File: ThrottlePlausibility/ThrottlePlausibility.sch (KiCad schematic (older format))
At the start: 18 parts, among them U1 MCP6004, U2 LM339, U3 74LS08, U4 74LS08, U5 LM339, U6 TLP222A

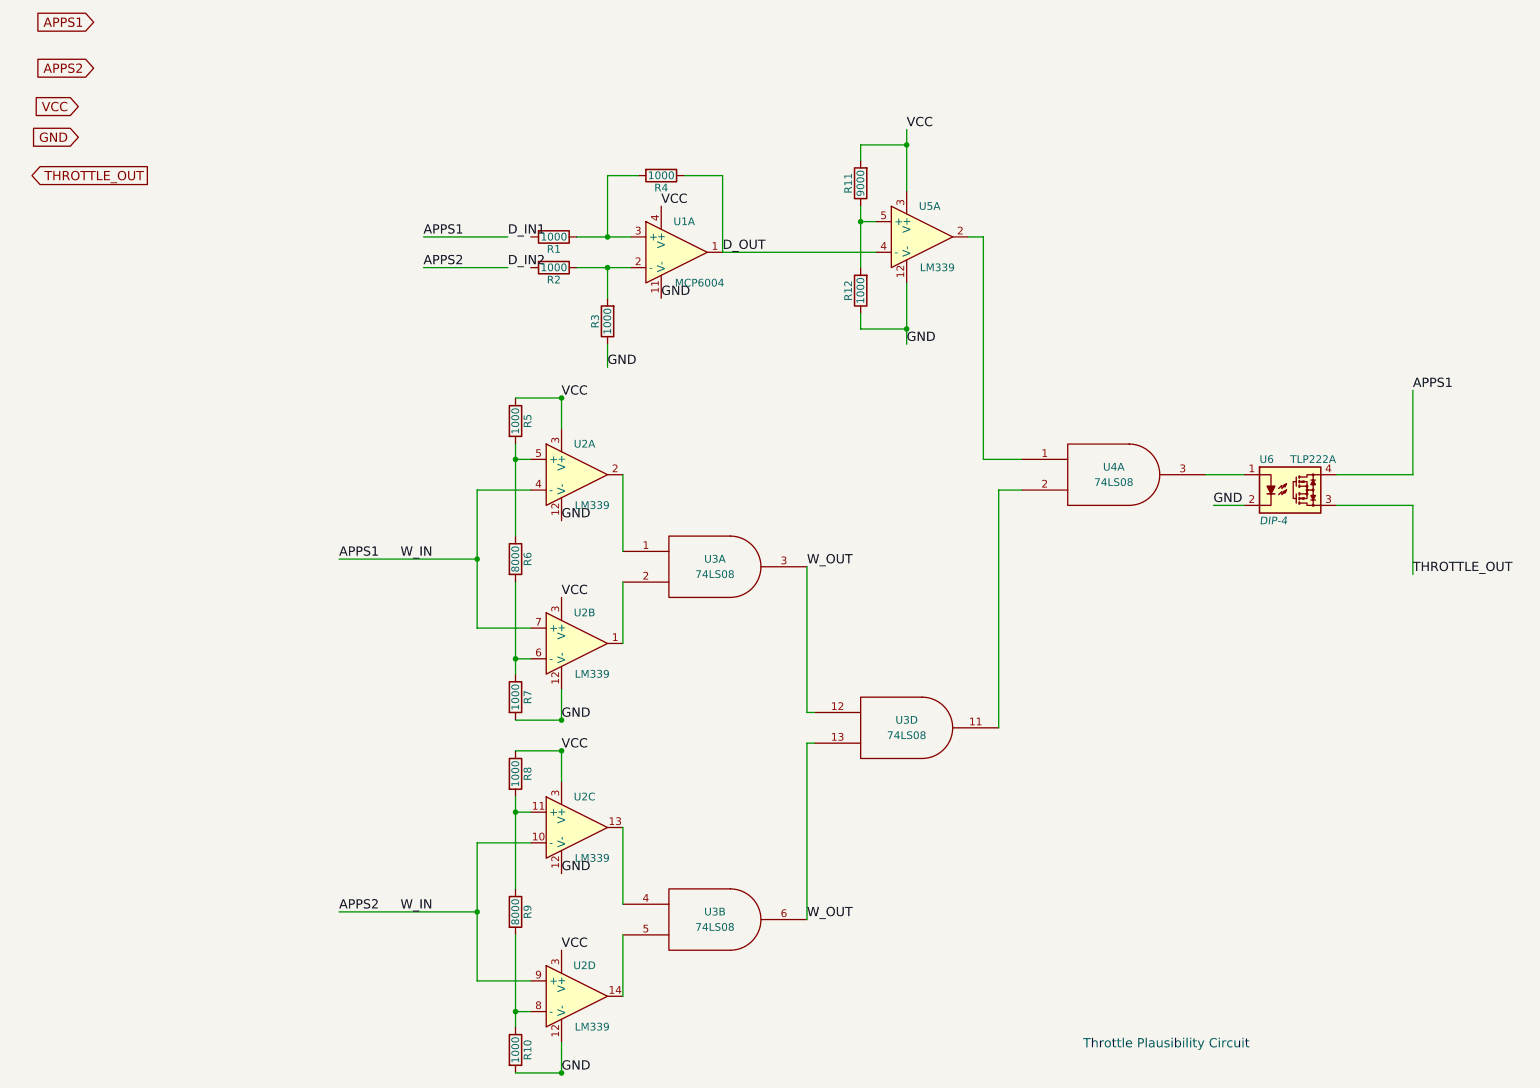
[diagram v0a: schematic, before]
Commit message: added SPICE model
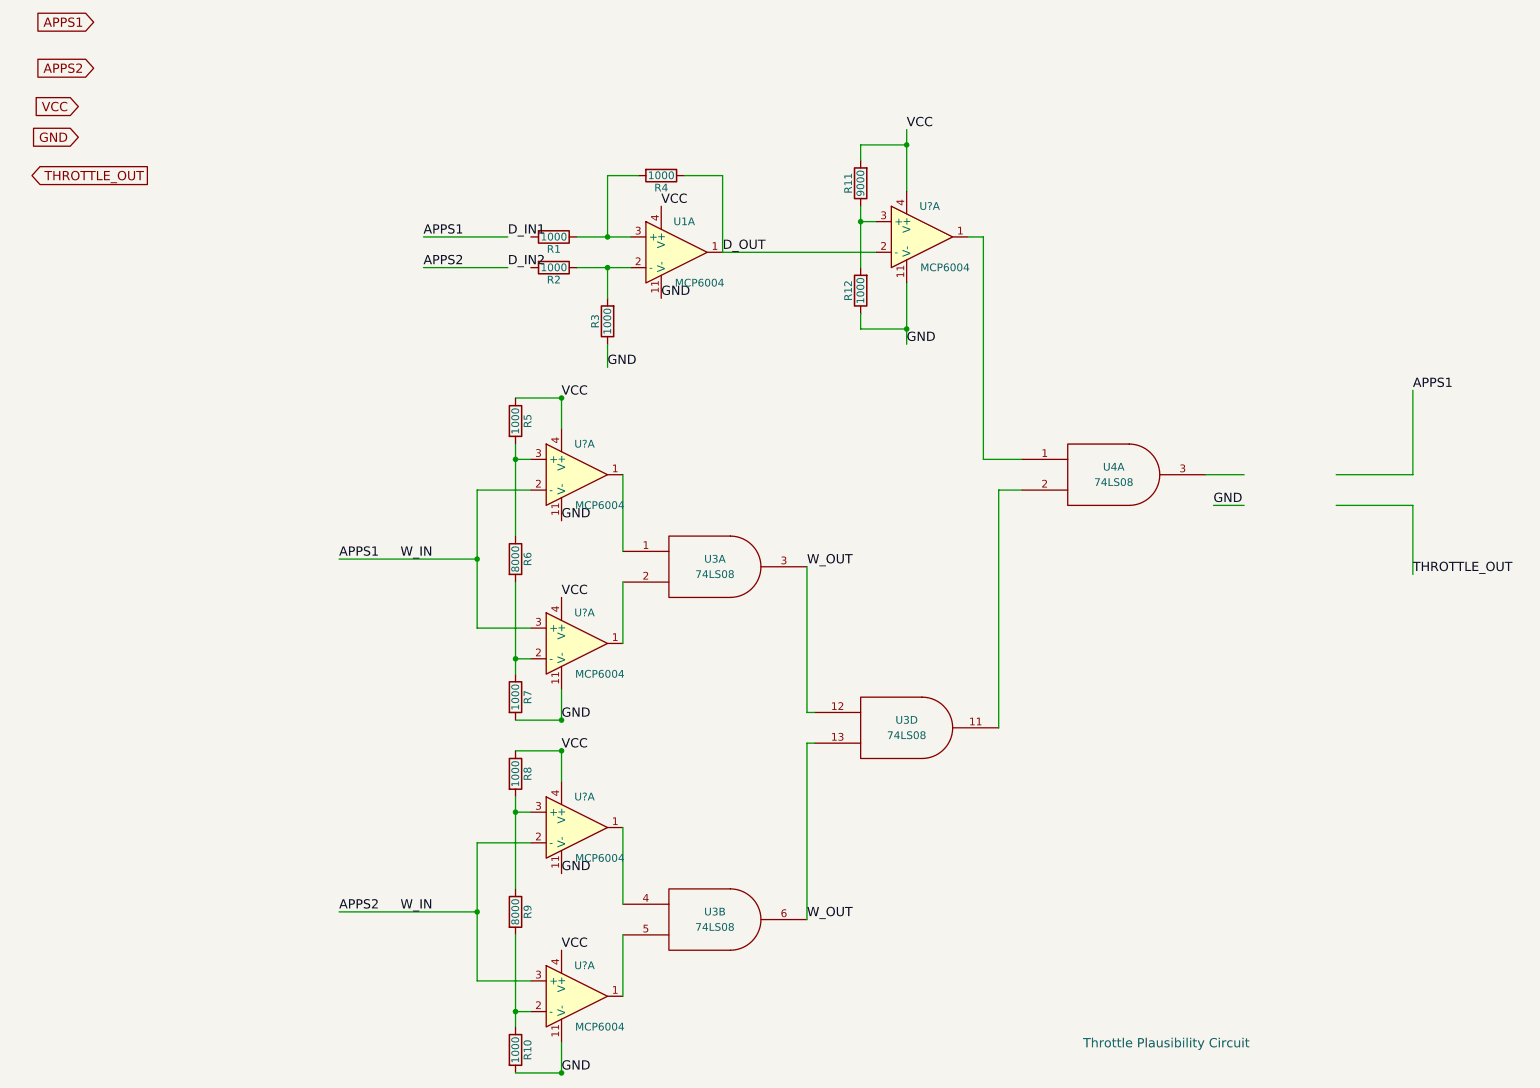
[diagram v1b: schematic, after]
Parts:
- removed U2, U5: LM339, symbol LM339
- removed U6: TLP222A, DIP-4, symbol TLP222A
- added U? (x5): MCP6004, symbol MCP6004
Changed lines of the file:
@@
 Text Label 3100 2400 0    60   ~ 0
 APPS2
-$Comp
-L LM339 U5
-U 1 1 589C6EA7
-P 6350 2200
-F 0 "U5" H 6400 2400 50  0000 C CNN
-F 1 "LM339" H 6450 2000 50  0000 C CNN
-F 2 "" H 6300 2300 50  0000 C CNN
-F 3 "" H 6400 2400 50  0000 C CNN
-	1    6350 2200
-	1    0    0    -1
-$EndComp
-$Comp
-L LM339 U2
-U 2 1 589C9450
-P 4100 4850
-F 0 "U2" H 4150 5050 50  0000 C CNN
-F 1 "LM339" H 4200 4650 50  0000 C CNN
-F 2 "" H 4050 4950 50  0000 C CNN
-F 3 "" H 4150 5050 50  0000 C CNN
-	2    4100 4850
-	1    0    0    -1
-$EndComp
-$Comp
-L LM339 U2
-U 1 1 589C95FE
-P 4100 3750
-F 0 "U2" H 4150 3950 50  0000 C CNN
-F 1 "LM339" H 4200 3550 50  0000 C CNN
-F 2 "" H 4050 3850 50  0000 C CNN
-F 3 "" H 4150 3950 50  0000 C CNN
-	1    4100 3750
-	1    0    0    -1
-$EndComp
-$Comp
-L LM339 U2
-U 3 1 589C96D1
-P 4100 6050
-F 0 "U2" H 4150 6250 50  0000 C CNN
-F 1 "LM339" H 4200 5850 50  0000 C CNN
-F 2 "" H 4050 6150 50  0000 C CNN
-F 3 "" H 4150 6250 50  0000 C CNN
-	3    4100 6050
-	1    0    0    -1
-$EndComp
-$Comp
-L LM339 U2
-U 4 1 589C974C
-P 4100 7150
-F 0 "U2" H 4150 7350 50  0000 C CNN
-F 1 "LM339" H 4200 6950 50  0000 C CNN
-F 2 "" H 4050 7250 50  0000 C CNN
-F 3 "" H 4150 7350 50  0000 C CNN
-	4    4100 7150
-	1    0    0    -1
-$EndComp
-$Comp
-L TLP222A U6
-U 1 1 589CAD48
-P 8750 3850
-F 0 "U6" H 8550 4050 50  0000 L CNN
-F 1 "TLP222A" H 8750 4050 50  0000 L CNN
-F 2 "DIP-4" H 8550 3650 50  0000 L CIN
-F 3 "" H 8700 3850 50  0000 L CNN
-	1    8750 3850
-	1    0    0    -1
-$EndComp
 Wire Wire Line
 	6750 2200 6750 3650
@@
 Text GLabel 1300 1800 0    60   Output ~ 0
 THROTTLE_OUT
+$Comp
+L MCP6004 U?
+U 1 1 58A1CB70
+P 4100 3750
+F 0 "U?" H 4150 3950 50  0000 C CNN
+F 1 "MCP6004" H 4250 3550 50  0000 C CNN
+F 2 "" H 4050 3850 50  0000 C CNN
+F 3 "" H 4150 3950 50  0000 C CNN
+	1    4100 3750
+	1    0    0    -1
+$EndComp
+$Comp
+L MCP6004 U?
+U 1 1 58A1CCBC
+P 4100 4850
+F 0 "U?" H 4150 5050 50  0000 C CNN
+F 1 "MCP6004" H 4250 4650 50  0000 C CNN
+F 2 "" H 4050 4950 50  0000 C CNN
+F 3 "" H 4150 5050 50  0000 C CNN
+	1    4100 4850
+	1    0    0    -1
+$EndComp
+$Comp
+L MCP6004 U?
+U 1 1 58A1D021
+P 4100 6050
+F 0 "U?" H 4150 6250 50  0000 C CNN
+F 1 "MCP6004" H 4250 5850 50  0000 C CNN
+F 2 "" H 4050 6150 50  0000 C CNN
+F 3 "" H 4150 6250 50  0000 C CNN
+	1    4100 6050
+	1    0    0    -1
+$EndComp
+$Comp
+L MCP6004 U?
+U 1 1 58A1D0D5
+P 4100 7150
+F 0 "U?" H 4150 7350 50  0000 C CNN
+F 1 "MCP6004" H 4250 6950 50  0000 C CNN
+F 2 "" H 4050 7250 50  0000 C CNN
+F 3 "" H 4150 7350 50  0000 C CNN
+	1    4100 7150
+	1    0    0    -1
+$EndComp
+$Comp
+L MCP6004 U?
+U 1 1 58A1D98F
+P 6350 2200
+F 0 "U?" H 6400 2400 50  0000 C CNN
+F 1 "MCP6004" H 6500 2000 50  0000 C CNN
+F 2 "" H 6300 2300 50  0000 C CNN
+F 3 "" H 6400 2400 50  0000 C CNN
+	1    6350 2200
+	1    0    0    -1
+$EndComp
 $EndSCHEMATC

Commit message: started datasheet text file, altered throttle sch
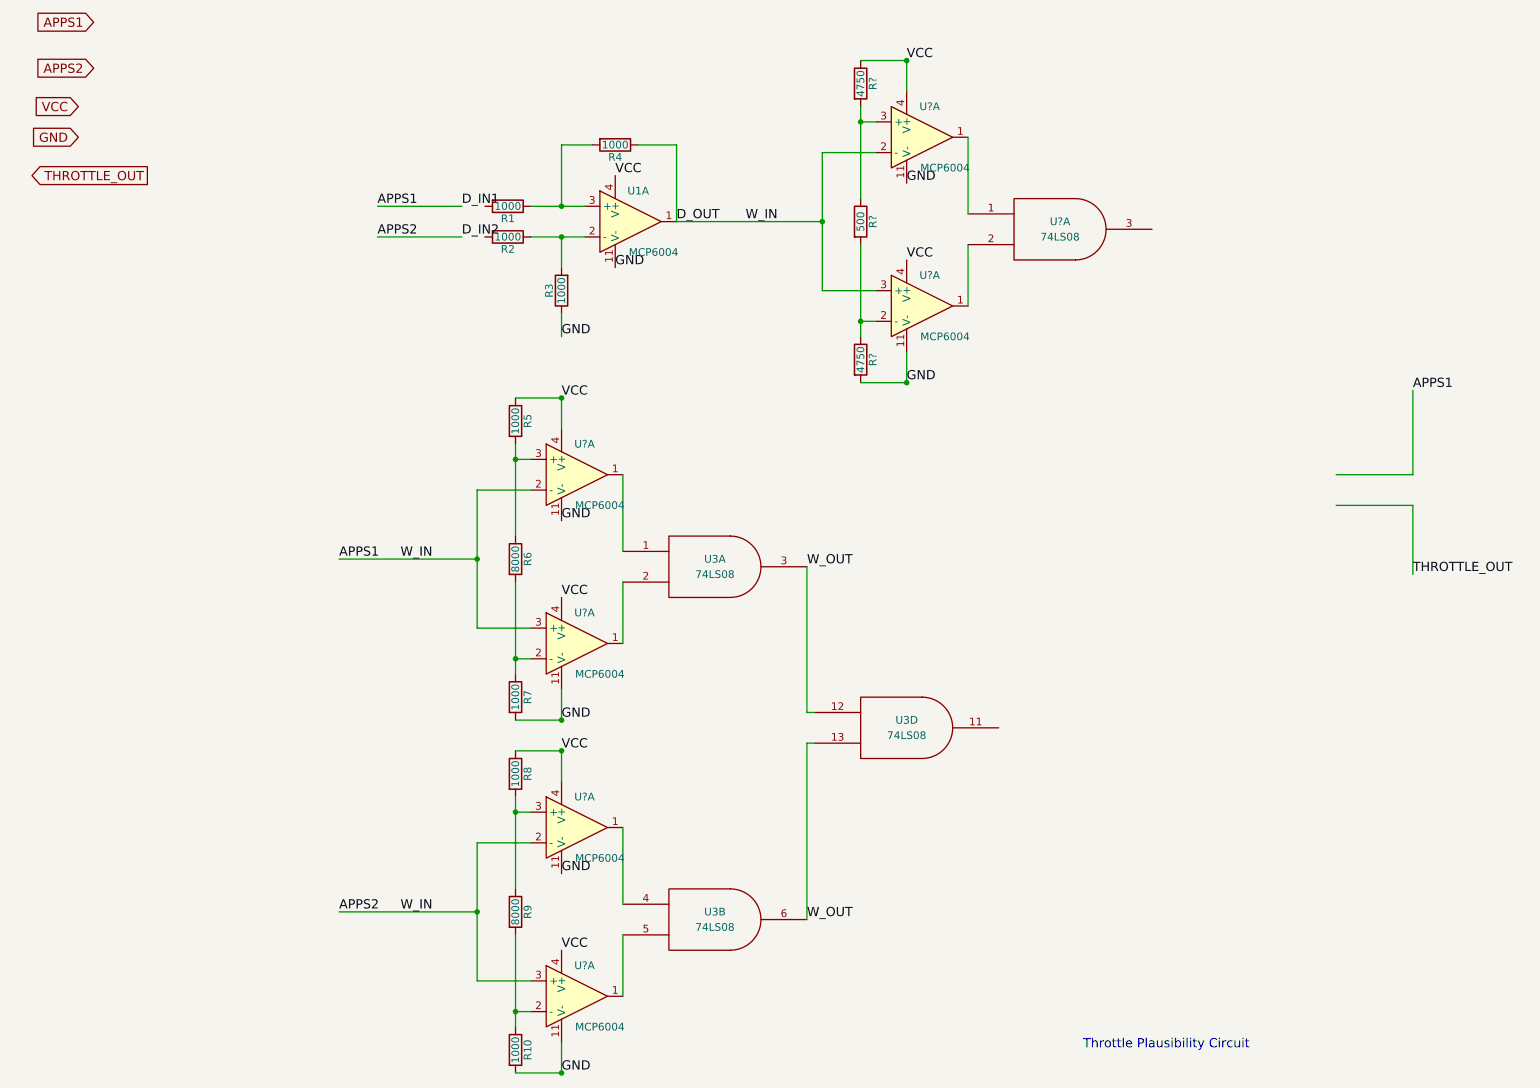
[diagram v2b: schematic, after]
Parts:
- removed R11: 9000, symbol R
- removed R12: 1000, symbol R
- removed U4: 74LS08, symbol 74LS08
- removed U?: MCP6004, symbol MCP6004
- added R? (x2): 4750, symbol R
- added R?: 500, symbol R
- added U?: 74LS08, symbol 74LS08
- added U? (x2): MCP6004, symbol MCP6004
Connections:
- wire segments 62 -> 60
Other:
- moved on the sheet: R1, R2, R3, R4, U1A
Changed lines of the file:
@@
 EESchema Schematic File Version 2
+LIBS:TSI_KiCad_Lib
 LIBS:power
 LIBS:device
@@
 L MCP6004 U1
 U 1 1 5897A753
-P 4750 2300
-F 0 "U1" H 4800 2500 50  0000 C CNN
-F 1 "MCP6004" H 4900 2100 50  0000 C CNN
-F 2 "" H 4700 2400 50  0000 C CNN
-F 3 "" H 4800 2500 50  0000 C CNN
-	1    4750 2300
+P 4450 2100
+F 0 "U1" H 4500 2300 50  0000 C CNN
+F 1 "MCP6004" H 4600 1900 50  0000 C CNN
+F 2 "" H 4400 2200 50  0000 C CNN
+F 3 "" H 4500 2300 50  0000 C CNN
+	1    4450 2100
 	1    0    0    -1
 $EndComp
@@
 L R R1
 U 1 1 5897ADAF
-P 3950 2200
-F 0 "R1" V 4030 2200 50  0000 C CNN
-F 1 "1000" V 3950 2200 50  0000 C CNN
-F 2 "" V 3880 2200 50  0000 C CNN
-F 3 "" H 3950 2200 50  0000 C CNN
-	1    3950 2200
+P 3650 2000
+F 0 "R1" V 3730 2000 50  0000 C CNN
+F 1 "1000" V 3650 2000 50  0000 C CNN
+F 2 "" V 3580 2000 50  0000 C CNN
+F 3 "" H 3650 2000 50  0000 C CNN
+	1    3650 2000
 	0    1    1    0
 $EndComp
@@
 L R R2
 U 1 1 5897AE5B
-P 3950 2400
-F 0 "R2" V 4030 2400 50  0000 C CNN
-F 1 "1000" V 3950 2400 50  0000 C CNN
-F 2 "" V 3880 2400 50  0000 C CNN
-F 3 "" H 3950 2400 50  0000 C CNN
-	1    3950 2400
+P 3650 2200
+F 0 "R2" V 3730 2200 50  0000 C CNN
+F 1 "1000" V 3650 2200 50  0000 C CNN
+F 2 "" V 3580 2200 50  0000 C CNN
+F 3 "" H 3650 2200 50  0000 C CNN
+	1    3650 2200
 	0    1    1    0
 $EndComp
@@
 L R R4
 U 1 1 5897AEA9
-P 4650 1800
-F 0 "R4" V 4730 1800 50  0000 C CNN
-F 1 "1000" V 4650 1800 50  0000 C CNN
-F 2 "" V 4580 1800 50  0000 C CNN
-F 3 "" H 4650 1800 50  0000 C CNN
-	1    4650 1800
+P 4350 1600
+F 0 "R4" V 4430 1600 50  0000 C CNN
+F 1 "1000" V 4350 1600 50  0000 C CNN
+F 2 "" V 4280 1600 50  0000 C CNN
+F 3 "" H 4350 1600 50  0000 C CNN
+	1    4350 1600
 	0    1    1    0
 $EndComp
@@
 L R R3
 U 1 1 5897AF3A
-P 4300 2750
-F 0 "R3" V 4380 2750 50  0000 C CNN
-F 1 "1000" V 4300 2750 50  0000 C CNN
-F 2 "" V 4230 2750 50  0000 C CNN
-F 3 "" H 4300 2750 50  0000 C CNN
-	1    4300 2750
+P 4000 2550
+F 0 "R3" V 4080 2550 50  0000 C CNN
+F 1 "1000" V 4000 2550 50  0000 C CNN
+F 2 "" V 3930 2550 50  0000 C CNN
+F 3 "" H 4000 2550 50  0000 C CNN
+	1    4000 2550
 	-1   0    0    1
 $EndComp
-Text Label 4650 2000 0    60   ~ 0
-VCC
-Text Label 4650 2600 0    60   ~ 0
-GND
-Text Label 5050 2300 0    60   ~ 0
+Text Label 4350 1800 0    60   ~ 0
+VCC
+Text Label 4350 2400 0    60   ~ 0
+GND
+Text Label 4750 2100 0    60   ~ 0
 D_OUT
-Text Label 3650 2200 0    60   ~ 0
+Text Label 3350 2000 0    60   ~ 0
 D_IN1
-Text Label 3650 2400 0    60   ~ 0
+Text Label 3350 2200 0    60   ~ 0
 D_IN2
-Text Label 4300 3050 0    60   ~ 0
-GND
-$Comp
-L 74LS08 U4
-U 1 1 589811F3
-P 7600 3750
-F 0 "U4" H 7600 3800 50  0000 C CNN
-F 1 "74LS08" H 7600 3700 50  0000 C CNN
-F 2 "" H 7600 3750 50  0000 C CNN
-F 3 "" H 7600 3750 50  0000 C CNN
-	1    7600 3750
-	1    0    0    -1
-$EndComp
+Text Label 4000 2850 0    60   ~ 0
+GND
 Text Label 2550 4300 0    60   ~ 0
 APPS1
@@
 Text Notes 7400 7500 0    60   ~ 0
 Throttle Plausibility Circuit
-$Comp
-L R R11
-U 1 1 5897769F
-P 5950 1850
-F 0 "R11" V 6030 1850 50  0000 C CNN
-F 1 "9000" V 5950 1850 50  0000 C CNN
-F 2 "" V 5880 1850 50  0000 C CNN
-F 3 "" H 5950 1850 50  0000 C CNN
-	1    5950 1850
-	-1   0    0    1
-$EndComp
-$Comp
-L R R12
-U 1 1 589777BD
-P 5950 2550
-F 0 "R12" V 6030 2550 50  0000 C CNN
-F 1 "1000" V 5950 2550 50  0000 C CNN
-F 2 "" V 5880 2550 50  0000 C CNN
-F 3 "" H 5950 2550 50  0000 C CNN
-	1    5950 2550
-	-1   0    0    1
-$EndComp
-Text Label 6250 1500 0    60   ~ 0
-VCC
-Text Label 6250 2900 0    60   ~ 0
-GND
 Connection ~ 3450 4300
 Wire Wire Line
@@
 	5600 5300 5650 5300
 Wire Wire Line
-	4100 2200 4450 2200
-Wire Wire Line
-	4100 2400 4450 2400
-Wire Wire Line
-	4300 2600 4300 2400
-Connection ~ 4300 2400
-Wire Wire Line
-	4500 1800 4300 1800
-Wire Wire Line
-	4300 1800 4300 2200
-Connection ~ 4300 2200
-Wire Wire Line
-	4800 1800 5050 1800
-Wire Wire Line
-	5050 1800 5050 2300
-Wire Wire Line
-	4300 2900 4300 3050
-Wire Wire Line
-	5950 2000 5950 2400
-Wire Wire Line
-	6050 2100 5950 2100
-Connection ~ 5950 2100
-Wire Wire Line
-	5950 1700 5950 1600
-Wire Wire Line
-	5950 2700 5950 2800
-Wire Wire Line
-	5050 2300 6050 2300
-Wire Wire Line
-	6250 2500 6250 2900
-Wire Wire Line
-	6250 1500 6250 1900
-Wire Wire Line
-	6650 2200 6750 2200
-Wire Wire Line
-	5950 1600 6250 1600
-Connection ~ 6250 1600
-Wire Wire Line
-	5950 2800 6250 2800
-Connection ~ 6250 2800
-Wire Wire Line
-	3650 2200 3100 2200
-Wire Wire Line
-	3650 2400 3100 2400
-Text Label 3100 2200 0    60   ~ 0
+	3800 2000 4150 2000
+Wire Wire Line
+	3800 2200 4150 2200
+Wire Wire Line
+	4000 2400 4000 2200
+Connection ~ 4000 2200
+Wire Wire Line
+	4200 1600 4000 1600
+Wire Wire Line
+	4000 1600 4000 2000
+Connection ~ 4000 2000
+Wire Wire Line
+	4500 1600 4750 1600
+Wire Wire Line
+	4750 1600 4750 2100
+Wire Wire Line
+	4000 2700 4000 2850
+Wire Wire Line
+	3350 2000 2800 2000
+Wire Wire Line
+	3350 2200 2800 2200
+Text Label 2800 2000 0    60   ~ 0
 APPS1
-Text Label 3100 2400 0    60   ~ 0
+Text Label 2800 2200 0    60   ~ 0
 APPS2
-Wire Wire Line
-	6750 2200 6750 3650
-Wire Wire Line
-	6750 3650 7000 3650
-Wire Wire Line
-	6850 5400 6850 3850
-Wire Wire Line
-	6850 3850 7000 3850
-Wire Wire Line
-	8200 3750 8450 3750
-Wire Wire Line
-	8450 3950 8250 3950
 Wire Wire Line
 	9050 3750 9550 3750
@@
 Text Label 9550 3200 0    60   ~ 0
 APPS1
-Text Label 8250 3950 0    60   ~ 0
-GND
 Text GLabel 1300 1800 0    60   Output ~ 0
 THROTTLE_OUT
@@
 $EndComp
 $Comp
+L R R?
+U 1 1 58A294BC
+P 5950 1200
+F 0 "R?" V 6030 1200 50  0000 C CNN
+F 1 "4750" V 5950 1200 50  0000 C CNN
+F 2 "" V 5880 1200 50  0000 C CNN
+F 3 "" H 5950 1200 50  0000 C CNN
+	1    5950 1200
+	1    0    0    -1
+$EndComp
+$Comp
+L R R?
+U 1 1 58A294C2
+P 5950 3000
+F 0 "R?" V 6030 3000 50  0000 C CNN
+F 1 "4750" V 5950 3000 50  0000 C CNN
+F 2 "" V 5880 3000 50  0000 C CNN
+F 3 "" H 5950 3000 50  0000 C CNN
+	1    5950 3000
+	1    0    0    -1
+$EndComp
+$Comp
+L R R?
+U 1 1 58A294C8
+P 5950 2100
+F 0 "R?" V 6030 2100 50  0000 C CNN
+F 1 "500" V 5950 2100 50  0000 C CNN
+F 2 "" V 5880 2100 50  0000 C CNN
+F 3 "" H 5950 2100 50  0000 C CNN
+	1    5950 2100
+	1    0    0    -1
+$EndComp
+$Comp
+L 74LS08 U?
+U 1 1 58A294CE
+P 7250 2150
+F 0 "U?" H 7250 2200 50  0000 C CNN
+F 1 "74LS08" H 7250 2100 50  0000 C CNN
+F 2 "" H 7250 2150 50  0000 C CNN
+F 3 "" H 7250 2150 50  0000 C CNN
+	1    7250 2150
+	1    0    0    -1
+$EndComp
+Text Label 6250 1050 0    60   ~ 0
+VCC
+Text Label 6250 3150 0    60   ~ 0
+GND
+Text Label 6250 1850 0    60   ~ 0
+GND
+Text Label 6250 2350 0    60   ~ 0
+VCC
+Text Label 5200 2100 0    60   ~ 0
+W_IN
+Connection ~ 5700 2100
+Wire Wire Line
+	5950 1950 5950 1350
+Wire Wire Line
+	5950 2250 5950 2850
+Wire Wire Line
+	6050 2750 5950 2750
+Connection ~ 5950 2750
+Wire Wire Line
+	6050 1450 5950 1450
+Connection ~ 5950 1450
+Wire Wire Line
+	5950 1050 6250 1050
+Wire Wire Line
+	6250 1050 6250 1250
+Wire Wire Line
+	5950 3150 6250 3150
+Wire Wire Line
+	6250 3150 6250 2950
+Wire Wire Line
+	5700 1650 5700 2550
+Wire Wire Line
+	5700 2550 6050 2550
+Wire Wire Line
+	5700 1650 6050 1650
+Wire Wire Line
+	6650 1550 6650 2050
+Wire Wire Line
+	6650 2650 6650 2250
+Connection ~ 6250 3150
+Connection ~ 6250 1050
+$Comp
 L MCP6004 U?
-U 1 1 58A1D98F
-P 6350 2200
-F 0 "U?" H 6400 2400 50  0000 C CNN
-F 1 "MCP6004" H 6500 2000 50  0000 C CNN
-F 2 "" H 6300 2300 50  0000 C CNN
-F 3 "" H 6400 2400 50  0000 C CNN
-	1    6350 2200
-	1    0    0    -1
-$EndComp
+U 1 1 58A294ED
+P 6350 1550
+F 0 "U?" H 6400 1750 50  0000 C CNN
+F 1 "MCP6004" H 6500 1350 50  0000 C CNN
+F 2 "" H 6300 1650 50  0000 C CNN
+F 3 "" H 6400 1750 50  0000 C CNN
+	1    6350 1550
+	1    0    0    -1
+$EndComp
+$Comp
+L MCP6004 U?
+U 1 1 58A294F3
+P 6350 2650
+F 0 "U?" H 6400 2850 50  0000 C CNN
+F 1 "MCP6004" H 6500 2450 50  0000 C CNN
+F 2 "" H 6300 2750 50  0000 C CNN
+F 3 "" H 6400 2850 50  0000 C CNN
+	1    6350 2650
+	1    0    0    -1
+$EndComp
+Wire Wire Line
+	4750 2100 5700 2100
 $EndSCHEMATC
